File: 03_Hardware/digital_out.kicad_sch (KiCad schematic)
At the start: 0 parts

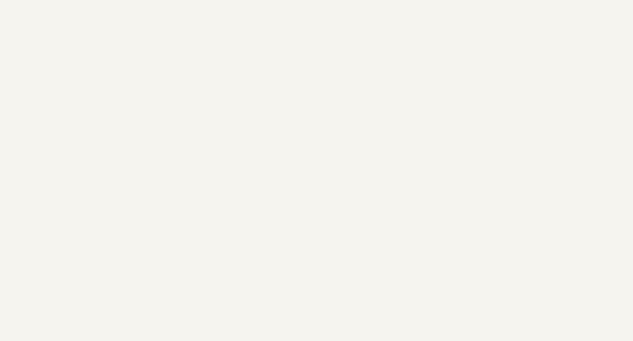
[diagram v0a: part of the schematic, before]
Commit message: TVS Dioden für Signal und DS18b20 hinzugefügt
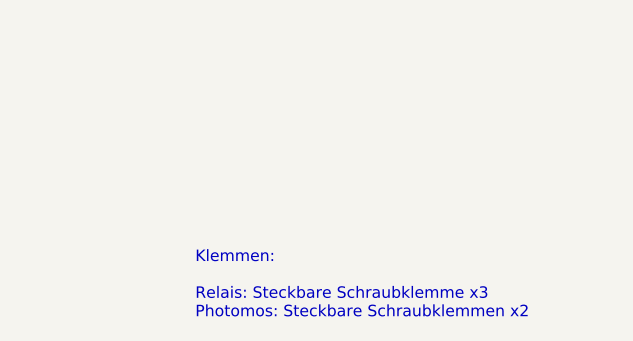
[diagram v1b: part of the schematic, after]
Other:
- note added: "Klemmen: Relais: Steckbare Schraubklemme x3 Photomos: Steckbare Schraubklemmen x2"
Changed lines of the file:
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@@
     (comment 2 "Sven Schneider")
+  )
+  (text "Klemmen: \n\nRelais: Steckbare Schraubklemme x3\nPhotomos: Steckbare Schraubklemmen x2"
+    (at 129.54 106.68 0)
+    (effects (font (size 1.27 1.27)) (justify left bottom))
   )
   (hierarchical_label "R1_Alarm" (shape input) (at 50.8 68.58 0) (fields_autoplaced)

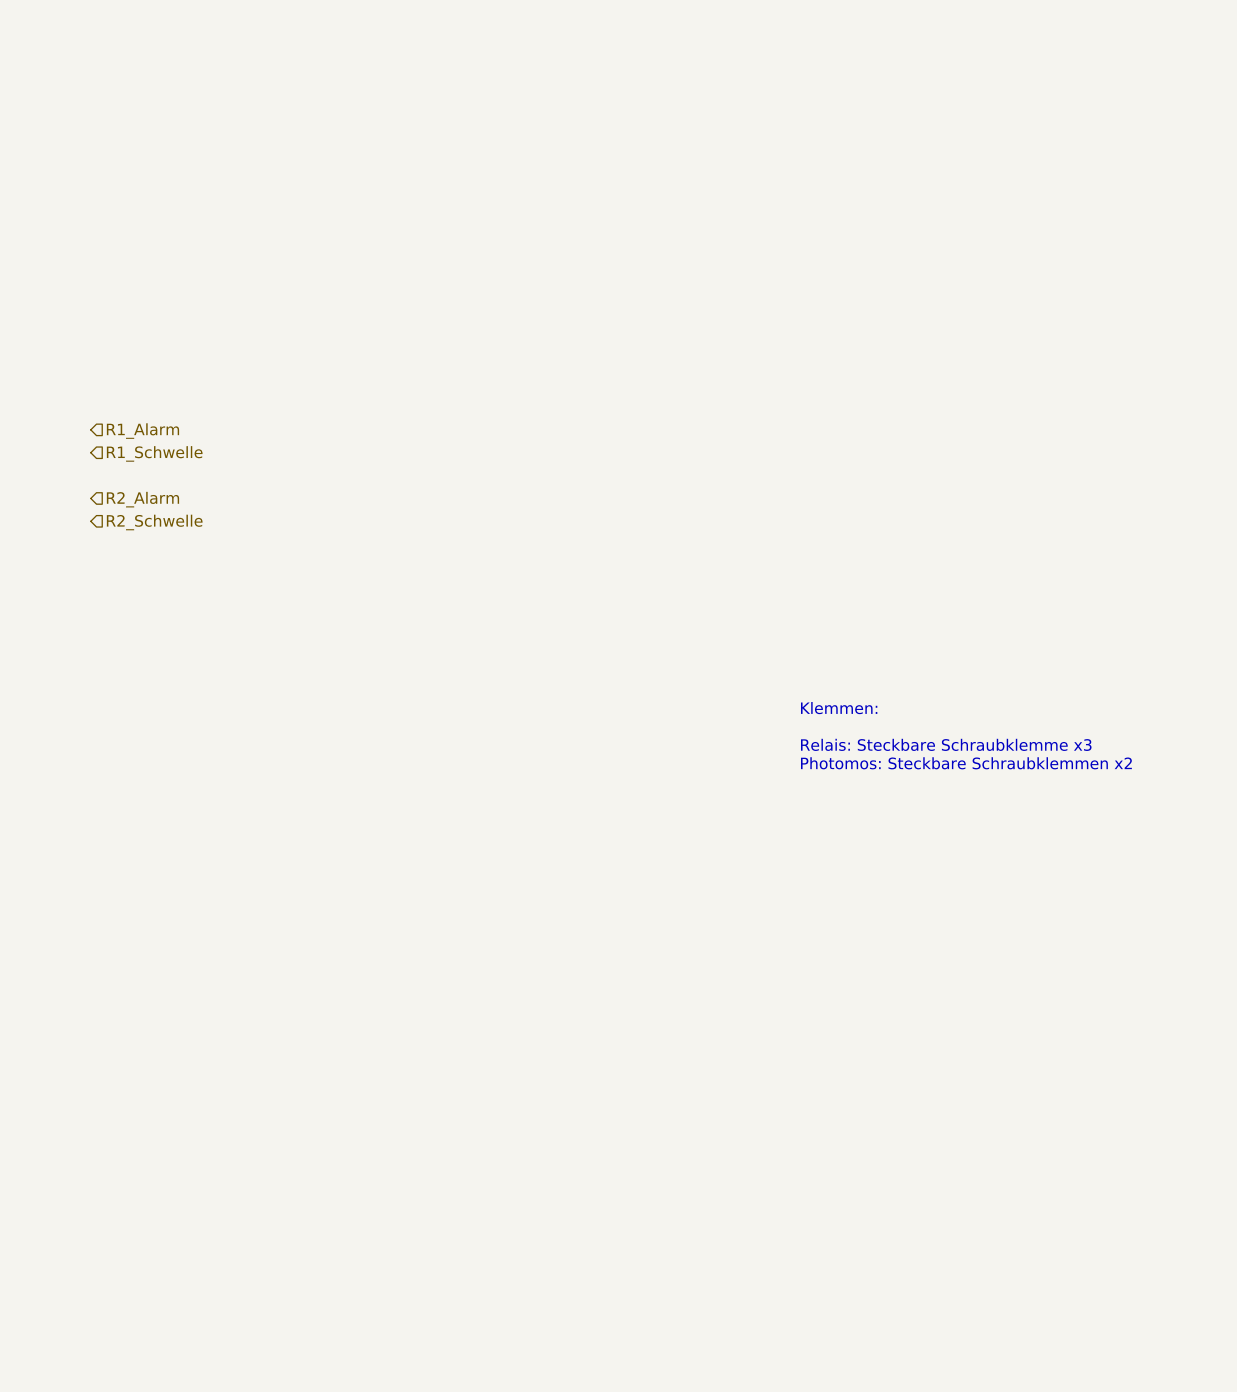
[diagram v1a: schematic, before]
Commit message: Relais und Photomos eingefügt. TODO: Schraubklemmen!
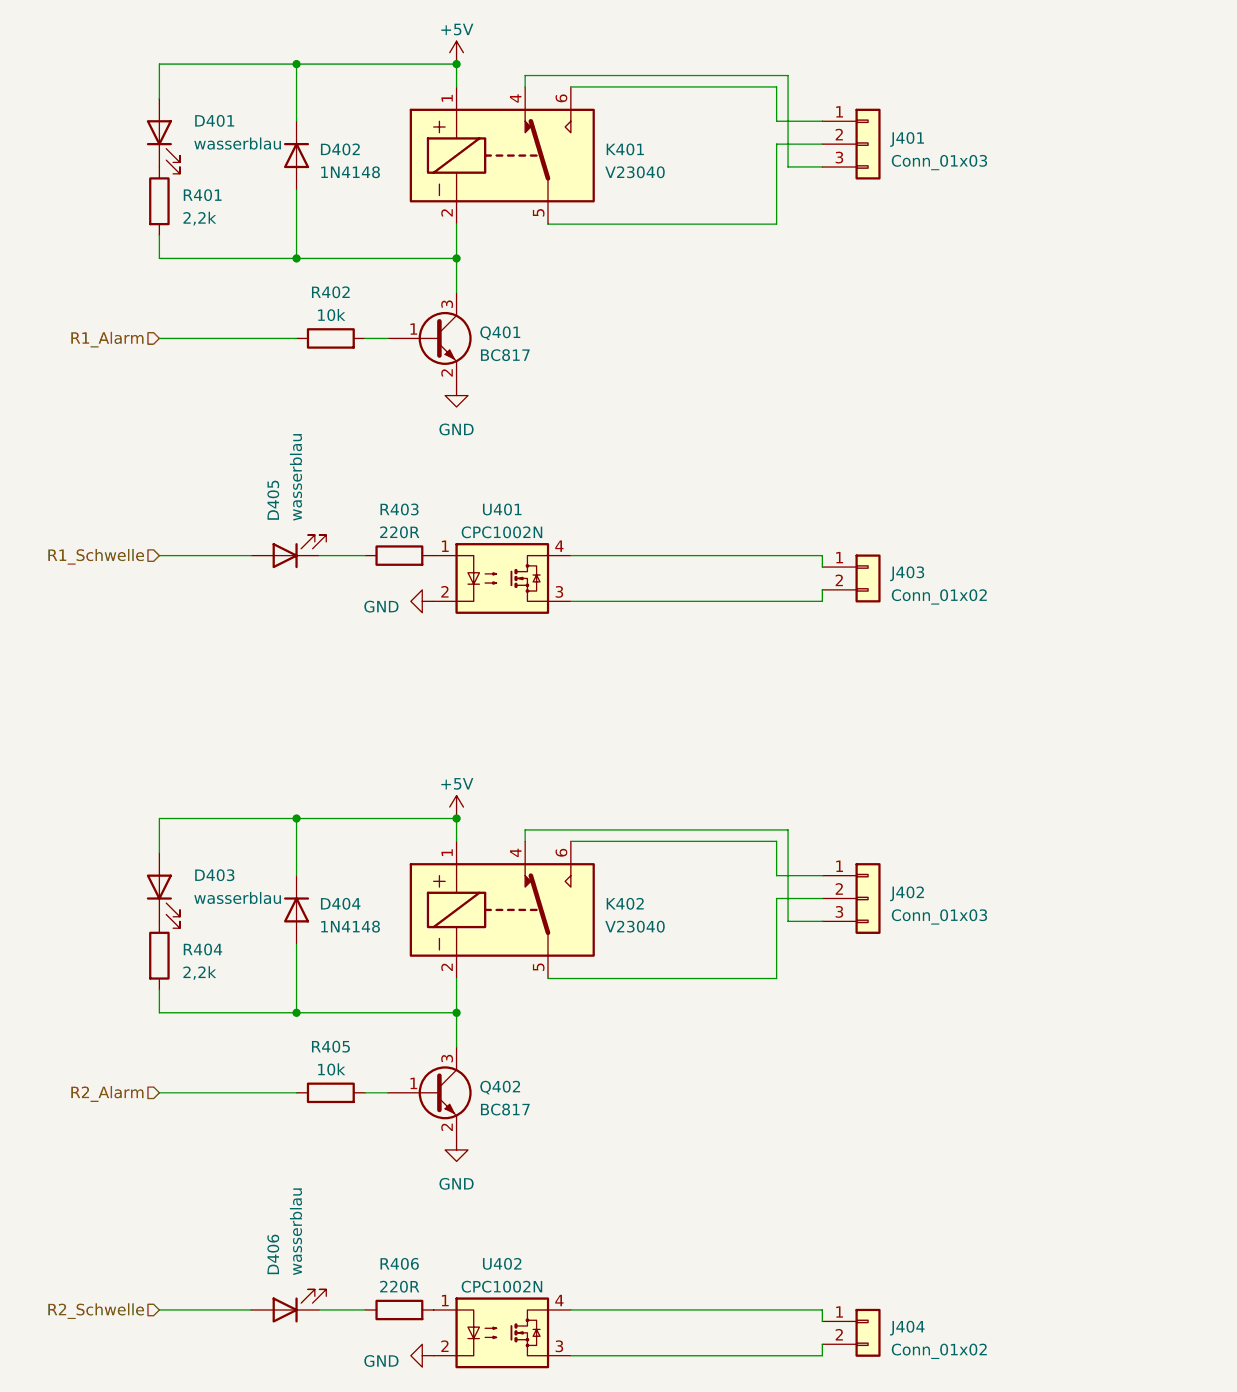
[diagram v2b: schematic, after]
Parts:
- added D401, D403, D405, D406: wasserblau, LED_SMD:LED_0603_1608Metric, symbol Device:LED
- added D402, D404: 1N4148, Diode_SMD:D_MiniMELF, symbol Diode:1N4148
- added J401, J402: Conn_01x03, symbol Connector_Generic:Conn_01x03
- added J403, J404: Conn_01x02, symbol Connector_Generic:Conn_01x02
- added K401, K402: V23040, board:V23040, symbol BMS_master:V23040
- added Q401, Q402: BC817, Package_TO_SOT_SMD:SOT-23, symbol Transistor_BJT:BC817
- added R401, R404: 2,2k, Resistor_SMD:R_0603_1608Metric, symbol Device:R
- added R402, R405: 10k, Resistor_SMD:R_0603_1608Metric, symbol Device:R
- added R403, R406: 220R, Resistor_SMD:R_0603_1608Metric, symbol Device:R
- added U401, U402: CPC1002N, Package_SO:SOP-4_3.8x4.1mm_P2.54mm, symbol Relay_SolidState:CPC1002N
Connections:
- net R1_Alarm: now also R402.1
- net R1_Schwelle: now also D405.2 (A)
- net R2_Alarm: now also R405.1
- net R2_Schwelle: now also D406.2 (A)
- new net: J401.1 (Pin_1), K401.6
- new net: J401.2 (Pin_2), K401.5
- new net: J401.3 (Pin_3), K401.4
- new net: D405.1 (K), R403.1
- new net: D401.1 (K), R401.1
- new net: D402.2 (A), K401.2, Q401.3 (C), R401.2
- new net: D404.2 (A), K402.2, Q402.3 (C), R404.2
- new net: Q401.1 (B), R402.2
- new net: Q402.1 (B), R405.2
- new net: R403.2, U401.1
- new net: J403.2 (Pin_2), U401.3
- new net: J403.1 (Pin_1), U401.4
- new net: J404.1 (Pin_1), U402.4
- new net: J404.2 (Pin_2), U402.3
- new net: J402.1 (Pin_1), K402.6
- new net: J402.2 (Pin_2), K402.5
- new net: J402.3 (Pin_3), K402.4
- new net: D406.1 (K), R406.1
- new net: R406.2, U402.1
- new net: D403.1 (K), R404.1
- new net +5V: D401.2 (A), D402.1 (K), D403.2 (A), D404.1 (K), K401.1, K402.1
- new net GND: Q401.2 (E), Q402.2 (E), U401.2, U402.2
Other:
- note removed: "Klemmen: Relais: Steckbare Schraubklemme x3 Photomos: Steckbare Schraubklemmen x2"

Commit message: Stecker fertig ausgewählt und Layout etwa 60% fertig
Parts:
- J401, J402: footprint (none) -> Connector_Wago:Wago_734-133_1x03_P3.50mm_Vertical
- J403, J404: footprint (none) -> Connector_Wago:Wago_734-132_1x02_P3.50mm_Vertical
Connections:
- net at U401.3: now also J403.1 (Pin_1); no longer J403.2 (Pin_2)
- net at U401.4: now also J403.2 (Pin_2); no longer J403.1 (Pin_1)
- net at J404.1 (Pin_1): now also U402.3; no longer U402.4
- net at J404.2 (Pin_2): now also U402.4; no longer U402.3
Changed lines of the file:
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@@
       (effects (font (size 1.27 1.27)) (justify left))
     )
-    (property "Footprint" "" (at 137.16 36.83 0)
+    (property "Footprint" "Connector_Wago:Wago_734-133_1x03_P3.50mm_Vertical" (at 137.16 36.83 0)
       (effects (font (size 1.27 1.27)) hide)
     )
@@
     )
   )
-  (symbol (lib_id "Connector_Generic:Conn_01x02") (at 137.16 167.64 0) (unit 1)
-    (in_bom yes) (on_board yes) (dnp no) (fields_autoplaced)
-    (property "Reference" "J404" (at 139.7 168.275 0)
-      (effects (font (size 1.27 1.27)) (justify left))
-    )
-    (property "Value" "Conn_01x02" (at 139.7 170.815 0)
-      (effects (font (size 1.27 1.27)) (justify left))
-    )
-    (property "Footprint" "" (at 137.16 167.64 0)
-      (effects (font (size 1.27 1.27)) hide)
-    )
-    (property "Datasheet" "~" (at 137.16 167.64 0)
+  (symbol (lib_id "Connector_Generic:Conn_01x02") (at 137.16 170.18 0) (mirror x) (unit 1)
+    (in_bom yes) (on_board yes) (dnp no)
+    (property "Reference" "J404" (at 139.7 169.545 0)
+      (effects (font (size 1.27 1.27)) (justify left))
+    )
+    (property "Value" "Conn_01x02" (at 139.7 167.005 0)
+      (effects (font (size 1.27 1.27)) (justify left))
+    )
+    (property "Footprint" "Connector_Wago:Wago_734-132_1x02_P3.50mm_Vertical" (at 137.16 170.18 0)
+      (effects (font (size 1.27 1.27)) hide)
+    )
+    (property "Datasheet" "~" (at 137.16 170.18 0)
       (effects (font (size 1.27 1.27)) hide)
     )
@@
       (effects (font (size 1.27 1.27)) (justify left))
     )
-    (property "Footprint" "" (at 137.16 120.65 0)
+    (property "Footprint" "Connector_Wago:Wago_734-133_1x03_P3.50mm_Vertical" (at 137.16 120.65 0)
       (effects (font (size 1.27 1.27)) hide)
     )
@@
     )
   )
-  (symbol (lib_id "Connector_Generic:Conn_01x02") (at 137.16 83.82 0) (unit 1)
-    (in_bom yes) (on_board yes) (dnp no) (fields_autoplaced)
-    (property "Reference" "J403" (at 139.7 84.455 0)
-      (effects (font (size 1.27 1.27)) (justify left))
-    )
-    (property "Value" "Conn_01x02" (at 139.7 86.995 0)
-      (effects (font (size 1.27 1.27)) (justify left))
-    )
-    (property "Footprint" "" (at 137.16 83.82 0)
-      (effects (font (size 1.27 1.27)) hide)
-    )
-    (property "Datasheet" "~" (at 137.16 83.82 0)
-      (effects (font (size 1.27 1.27)) hide)
-    )
+  (symbol (lib_id "Connector_Generic:Conn_01x02") (at 137.16 86.36 0) (mirror x) (unit 1)
+    (in_bom yes) (on_board yes) (dnp no)
+    (property "Reference" "J403" (at 139.7 85.725 0)
+      (effects (font (size 1.27 1.27)) (justify left))
+    )
+    (property "Value" "Conn_01x02" (at 139.7 83.185 0)
+      (effects (font (size 1.27 1.27)) (justify left))
+    )
+    (property "Footprint" "Connector_Wago:Wago_734-132_1x02_P3.50mm_Vertical" (at 137.16 86.36 0)
+      (effects (font (size 1.27 1.27)) hide)
+    )
+    (property "Datasheet" "~" (at 137.16 86.36 0)
+      (effects (font (size 1.27 1.27)) hide)
+    )
